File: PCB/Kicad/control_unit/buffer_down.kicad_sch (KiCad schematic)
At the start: 2 parts, among them U13 74HC245, U24 74HC245

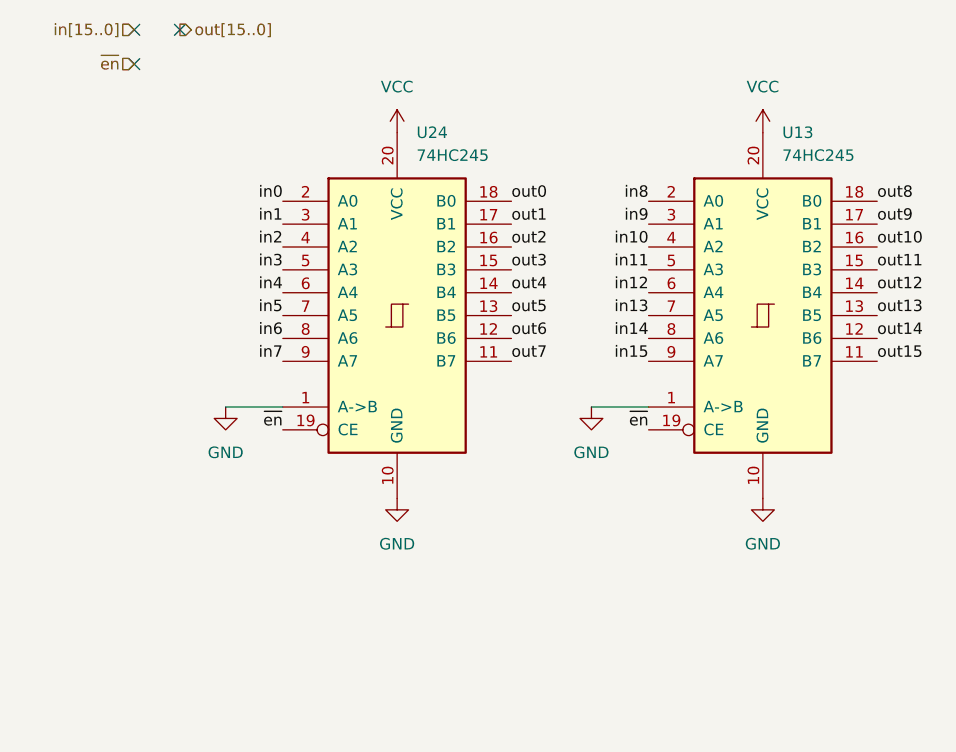
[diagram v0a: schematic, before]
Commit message: control unit schematic
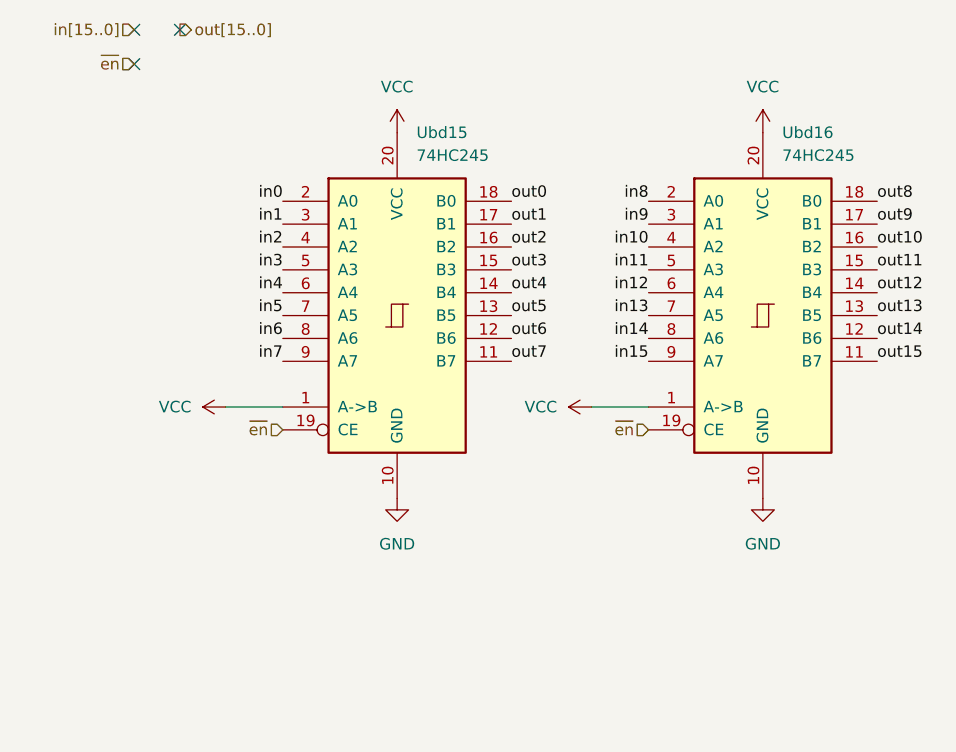
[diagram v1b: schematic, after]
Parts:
- removed U13: 74HC245, symbol 74xx:74HC245
- added Ubd16: 74HC245, Package_SO:SOIC-20W_7.5x12.8mm_P1.27mm, symbol 74xx:74HC245
- Ubd15: renamed from U24; footprint (none) -> Package_SO:SOIC-20W_7.5x12.8mm_P1.27mm
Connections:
- net GND: now also Ubd16.10 (GND); no longer Ubd15.1 (A->B)
- net VCC: now also Ubd15.1 (A->B), Ubd16.1 (A->B), Ubd16.20 (VCC)
- net in10: now also Ubd16.4 (A2)
- net in11: now also Ubd16.5 (A3)
- net in12: now also Ubd16.6 (A4)
- net in13: now also Ubd16.7 (A5)
- net in14: now also Ubd16.8 (A6)
- net in15: now also Ubd16.9 (A7)
- net in8: now also Ubd16.2 (A0)
- net in9: now also Ubd16.3 (A1)
- net out10: now also Ubd16.16 (B2)
- net out11: now also Ubd16.15 (B3)
- net out12: now also Ubd16.14 (B4)
- net out13: now also Ubd16.13 (B5)
- net out14: now also Ubd16.12 (B6)
- net out15: now also Ubd16.11 (B7)
- net out8: now also Ubd16.18 (B0)
- net out9: now also Ubd16.17 (B1)
- net ~{en}: now also Ubd16.19 (CE)
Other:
- company: (none) -> AGH Logic Unit
- title: (none) -> Buffer Top->Down

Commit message: control unit update
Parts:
- added Cbd2, Cbd28: 100nF, Capacitor_SMD:C_0402_1005Metric, symbol Device:C
- Ubd15, Ubd16: value 74HC245 -> 74245; footprint Package_SO:SOIC-20W_7.5x12.8mm_P1.27mm -> Package_SO:TSSOP-20_4.4x6.5mm_P0.65mm
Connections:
- net GND: now also Cbd2.2, Cbd28.2
- net VCC: now also Cbd2.1, Cbd28.1
